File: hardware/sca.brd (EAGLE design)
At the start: 87.6 x 73.3 mm, 38 parts

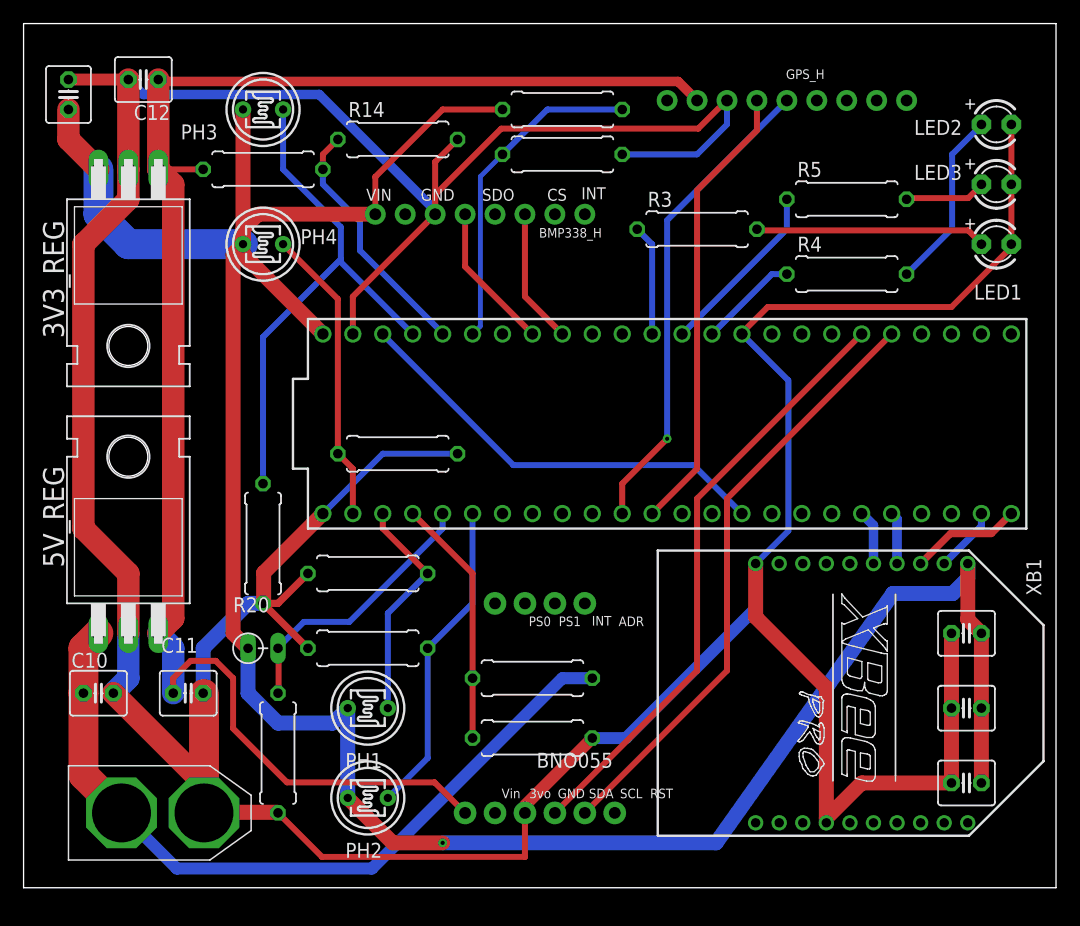
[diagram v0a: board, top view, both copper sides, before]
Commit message: corrected analog output pins
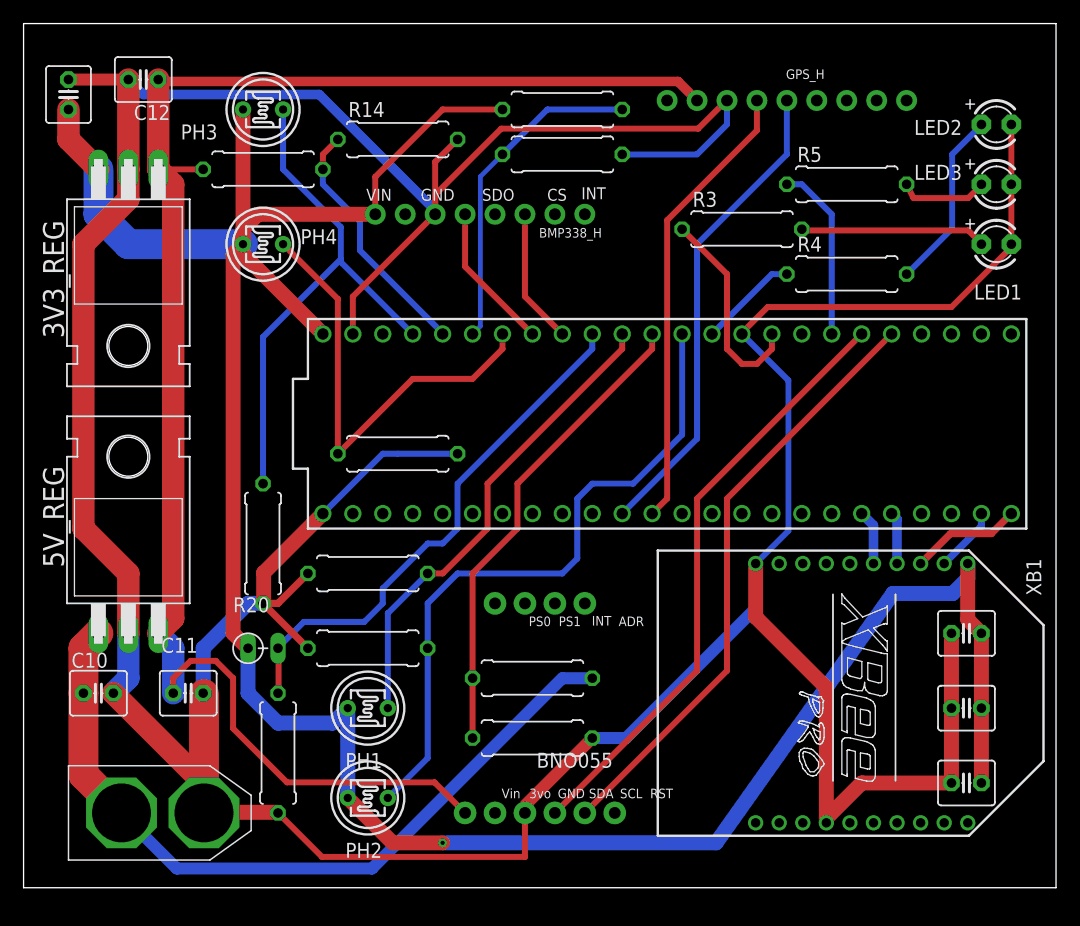
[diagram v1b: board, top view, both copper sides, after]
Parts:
- moved R3 3.81 mm to (61.0, 55.9)
- moved R5 1.27 mm to (69.8, 59.7)
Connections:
- net BATT_T: now also TEENSY3.6.17/A3; no longer TEENSY3.6.3
- net BATT_V: now also TEENSY3.6.15/A1; no longer TEENSY3.6.2
- net LED_1: now also TEENSY3.6.A22; no longer TEENSY3.6.15/A1
- net LED_3: now also TEENSY3.6.39/A20; no longer TEENSY3.6.14/A0
- net PR_1: now also TEENSY3.6.16/A2; no longer TEENSY3.6.1
- net PR_2: now also TEENSY3.6.14/A0; no longer TEENSY3.6.4
- net PR_4: now also TEENSY3.6.20/A6; no longer TEENSY3.6.0
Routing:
- net 3.3V: track 36.8 -> 0.00 mm
- net PR_2: track 27.1 -> 56.9 mm
- net BATT_T: track 23.3 -> 45.3 mm
- net PR_1: track 19.5 -> 40.7 mm
- net BATT_V: track 21.2 -> 40.6 mm
- net PR_4: track 25.3 -> 38.6 mm
- net LED_1: track 9.42 -> 17.9 mm
- net N$7: track 19.6 -> 15.8 mm
- net N$13: track 6.92 -> 7.58 mm
- net GPS_TX: vias 1 -> 0

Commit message: updated resistor values
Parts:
- R10, R6, R7, R8, R9: value 1M -> 10k
- R3, R4, R5: value 560 -> 1k
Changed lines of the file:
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@@
 <drawing>
 <settings>
-<setting alwaysvectorfont="no"/>
+<setting alwaysvectorfont="yes"/>
 <setting verticaltext="up"/>
 </settings>
@@
 </layers>
 <board>
-<fusionsync huburn="a.YnVzaW5lc3M6cGl0dDIxMA" projecturn="a.YnVzaW5lc3M6cGl0dDIxMCNEMjAxOTEwMTIyMjYwMjg0NTY" f3durn="urn:adsk.wipprod:dm.lineage:0fGlfKSVT8SH4LnvjsbdpQ" pcbguid="726667e8-dd8c-481c-944e-8e115b9bc285" lastpulledtime="" lastsyncedchangeguid="9d0e714c-d6f2-9322-4c5c-de335c59dd69"/>
+<fusionsync huburn="a.YnVzaW5lc3M6cGl0dDIxMA" projecturn="a.YnVzaW5lc3M6cGl0dDIxMCNEMjAxOTEwMTIyMjYwMjg0NTY" f3durn="urn:adsk.wipprod:dm.lineage:0fGlfKSVT8SH4LnvjsbdpQ" pcbguid="726667e8-dd8c-481c-944e-8e115b9bc285" lastpulledtime="" lastsyncedchangeguid="c9b7f4ff-d5ec-61ff-36d8-418587e66183"/>
 <plain>
 <wire x1="0" y1="0" x2="87.61" y2="0" width="0" layer="20"/>
@@
 <attribute name="VALUE" x="53.34" y="63.627" size="0.8128" layer="27"/>
 </element>
-<element name="R3" library="resistor" library_urn="urn:adsk.eagle:library:348" package="0309/10" package3d_urn="urn:adsk.eagle:package:23567/1" value="560" x="60.96" y="55.88" smashed="yes">
+<element name="R3" library="resistor" library_urn="urn:adsk.eagle:library:348" package="0309/10" package3d_urn="urn:adsk.eagle:package:23567/1" value="1k" x="60.96" y="55.88" smashed="yes">
 <attribute name="NAME" x="56.769" y="57.785" size="1.27" layer="25" ratio="10"/>
 <attribute name="VALUE" x="57.785" y="55.1942" size="1.27" layer="27" ratio="10"/>
 </element>
-<element name="R4" library="resistor" library_urn="urn:adsk.eagle:library:348" package="0309/10" package3d_urn="urn:adsk.eagle:package:23567/1" value="560" x="69.85" y="52.07" smashed="yes">
+<element name="R4" library="resistor" library_urn="urn:adsk.eagle:library:348" package="0309/10" package3d_urn="urn:adsk.eagle:package:23567/1" value="1k" x="69.85" y="52.07" smashed="yes">
 <attribute name="NAME" x="65.659" y="53.975" size="1.27" layer="25" ratio="10"/>
 <attribute name="VALUE" x="66.675" y="51.3842" size="1.27" layer="27" ratio="10"/>
@@
 <attribute name="VALUE" x="84.455" y="58.039" size="1.27" layer="27" ratio="10"/>
 </element>
-<element name="R5" library="resistor" library_urn="urn:adsk.eagle:library:348" package="0309/10" package3d_urn="urn:adsk.eagle:package:23567/1" value="560" x="69.85" y="59.69" smashed="yes">
+<element name="R5" library="resistor" library_urn="urn:adsk.eagle:library:348" package="0309/10" package3d_urn="urn:adsk.eagle:package:23567/1" value="1k" x="69.85" y="59.69" smashed="yes">
 <attribute name="NAME" x="65.659" y="61.595" size="1.27" layer="25" ratio="10"/>
 <attribute name="VALUE" x="66.675" y="59.0042" size="1.27" layer="27" ratio="10"/>
@@
 </element>
 <element name="U$5" library="XT60" package="XT60" value="XT60" x="3.81" y="6.35" smashed="yes"/>
-<element name="R6" library="resistor" library_urn="urn:adsk.eagle:library:348" package="0309/10" package3d_urn="urn:adsk.eagle:package:23567/1" value="1M" x="29.21" y="20.32" smashed="yes" rot="R180">
+<element name="R6" library="resistor" library_urn="urn:adsk.eagle:library:348" package="0309/10" package3d_urn="urn:adsk.eagle:package:23567/1" value="10k" x="29.21" y="20.32" smashed="yes" rot="R180">
 <attribute name="VALUE" x="32.385" y="21.0058" size="1.27" layer="27" ratio="10" rot="R180"/>
 </element>
-<element name="R7" library="resistor" library_urn="urn:adsk.eagle:library:348" package="0309/10" package3d_urn="urn:adsk.eagle:package:23567/1" value="1M" x="29.21" y="26.67" smashed="yes">
+<element name="R7" library="resistor" library_urn="urn:adsk.eagle:library:348" package="0309/10" package3d_urn="urn:adsk.eagle:package:23567/1" value="10k" x="29.21" y="26.67" smashed="yes">
 <attribute name="VALUE" x="26.035" y="25.9842" size="1.27" layer="27" ratio="10"/>
 </element>
-<element name="R8" library="resistor" library_urn="urn:adsk.eagle:library:348" package="0309/10" package3d_urn="urn:adsk.eagle:package:23567/1" value="1M" x="20.32" y="29.21" smashed="yes" rot="R270">
+<element name="R8" library="resistor" library_urn="urn:adsk.eagle:library:348" package="0309/10" package3d_urn="urn:adsk.eagle:package:23567/1" value="10k" x="20.32" y="29.21" smashed="yes" rot="R270">
 <attribute name="VALUE" x="19.6342" y="32.385" size="1.27" layer="27" ratio="10" rot="R270"/>
 </element>
-<element name="R9" library="resistor" library_urn="urn:adsk.eagle:library:348" package="0309/10" package3d_urn="urn:adsk.eagle:package:23567/1" value="1M" x="31.75" y="36.83" smashed="yes">
+<element name="R9" library="resistor" library_urn="urn:adsk.eagle:library:348" package="0309/10" package3d_urn="urn:adsk.eagle:package:23567/1" value="10k" x="31.75" y="36.83" smashed="yes">
 <attribute name="VALUE" x="28.575" y="36.1442" size="1.27" layer="28" ratio="10"/>
 </element>
-<element name="R10" library="resistor" library_urn="urn:adsk.eagle:library:348" package="0309/10" package3d_urn="urn:adsk.eagle:package:23567/1" value="1M" x="21.59" y="11.43" smashed="yes" rot="R90">
+<element name="R10" library="resistor" library_urn="urn:adsk.eagle:library:348" package="0309/10" package3d_urn="urn:adsk.eagle:package:23567/1" value="10k" x="21.59" y="11.43" smashed="yes" rot="R90">
 <attribute name="VALUE" x="22.2758" y="8.255" size="1.27" layer="27" ratio="10" rot="R90"/>
 </element>

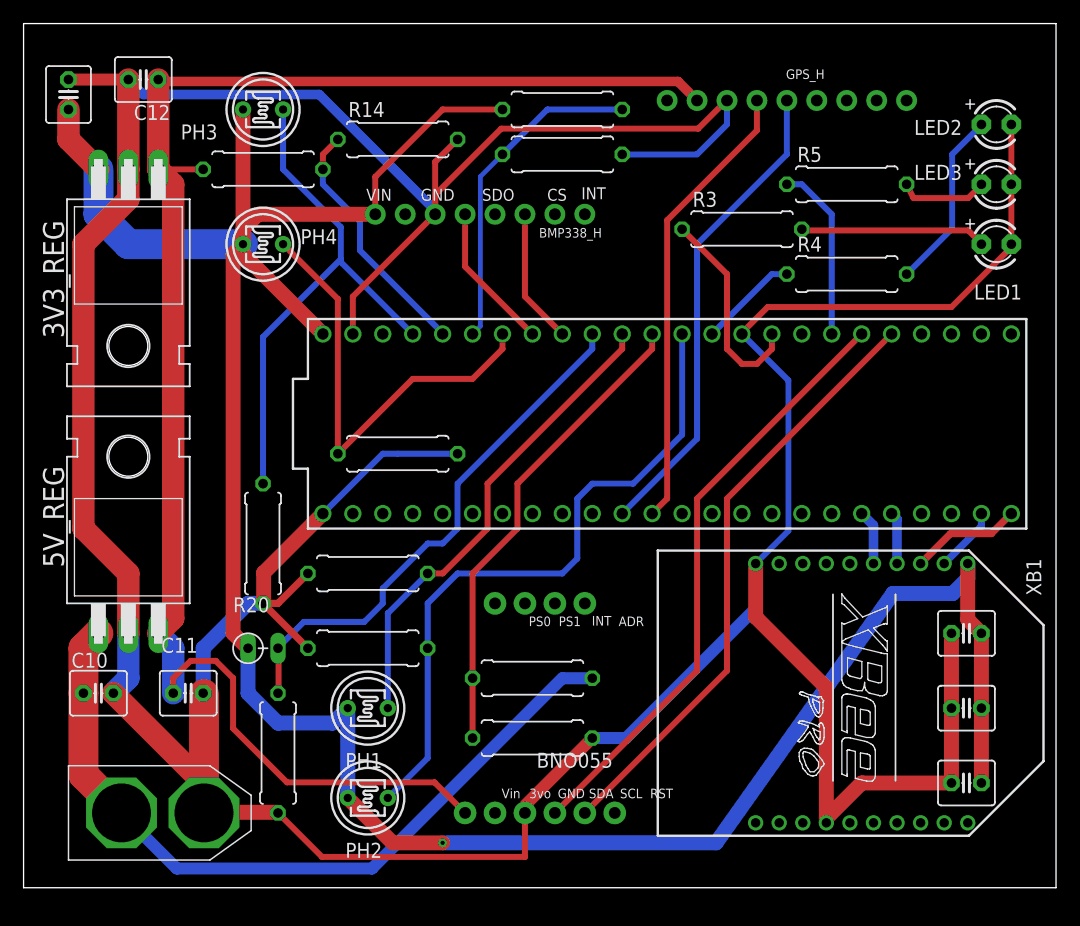
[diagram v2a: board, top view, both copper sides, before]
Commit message: made power traces 50 mil min
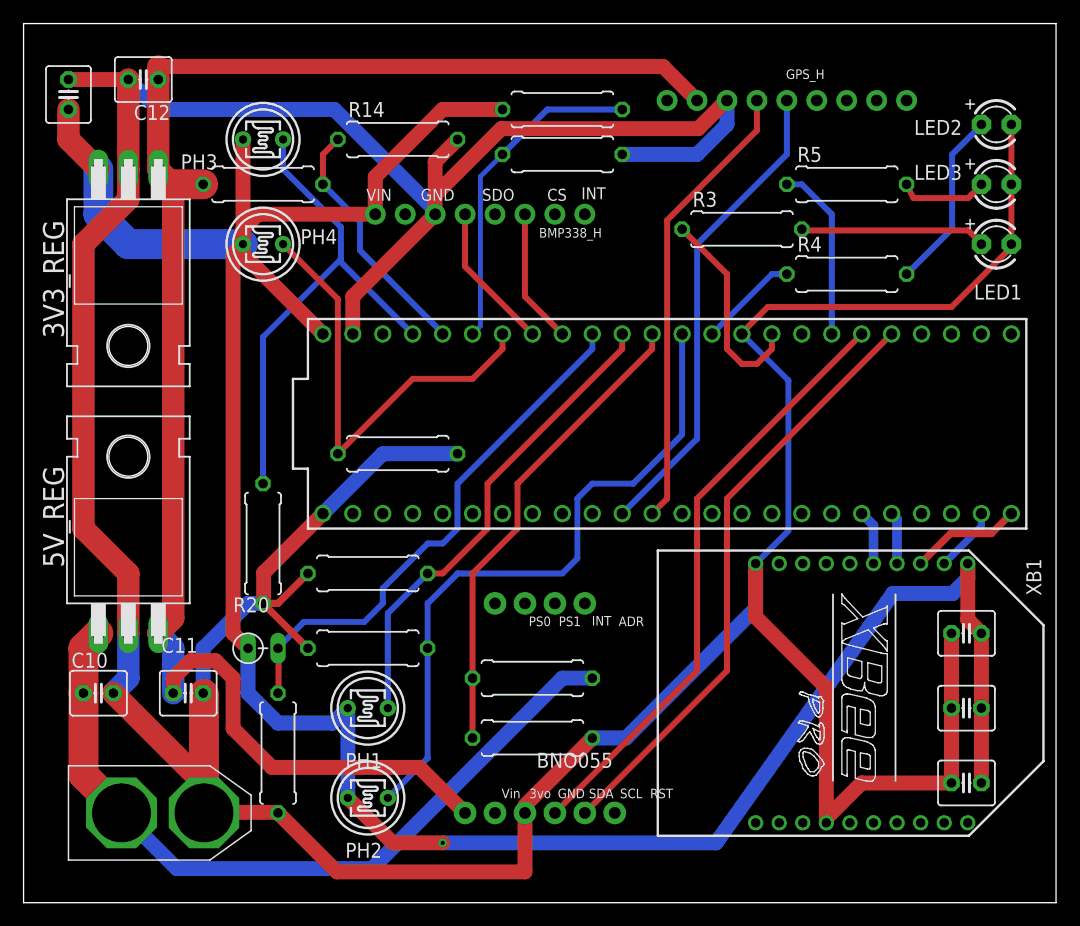
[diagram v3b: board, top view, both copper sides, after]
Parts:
- moved PH3 2.54 mm to (20.3, 63.5)
- moved R13 1.27 mm to (20.3, 59.7)
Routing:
- net +3V3: track 217.1 -> 214.6 mm
- net PR_3: track 45.4 -> 42.9 mm
- net GND: track 393.2 -> 394.9 mm
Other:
- board size 87.6 x 73.3 mm -> 87.6 x 74.6 mm
